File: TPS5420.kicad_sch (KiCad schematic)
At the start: 10 parts, among them U1 TPS5420D, U2 CDBC560-G

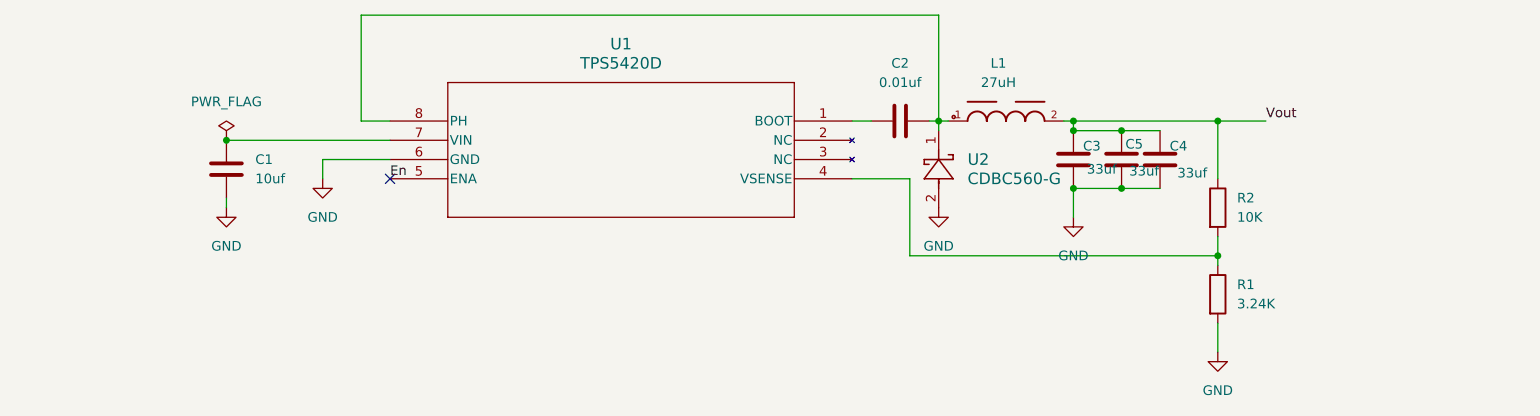
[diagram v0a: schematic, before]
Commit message: Added scre terminals
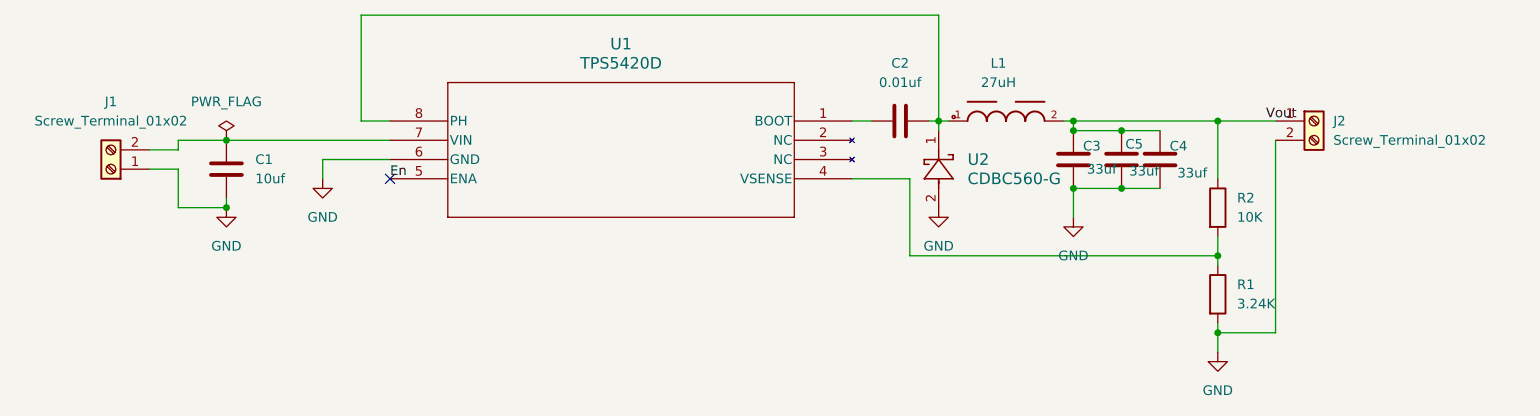
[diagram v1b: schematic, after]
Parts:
- added J1, J2: Screw_Terminal_01x02, TerminalBlock_RND:TerminalBlock_RND_205-00232_1x02_P5.08mm_Horizontal, symbol Connector:Screw_Terminal_01x02
- U2: footprint TPS5420_CADs:CDBC-G-M -> TPS5420_CADs:CDBC-G
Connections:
- net GND: now also J1.1 (Pin_1), J2.2 (Pin_2)
- net Vout: now also J2.1 (Pin_1)
- net at C1.1, U1.7 (VIN): now also J1.2 (Pin_2)
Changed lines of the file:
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@@
+	)
+	(junction
+		(at 50.8 111.76)
+		(diameter 0)
+		(color 0 0 0 0)
+	)
+	(junction
+		(at 181.61 128.27)
+		(diameter 0)
+		(color 0 0 0 0)
 	)
 	(junction
@@
 	(wire
 		(pts
+			(xy 40.64 106.68) (xy 44.45 106.68)
+		)
+		(stroke
+			(width 0)
+			(type default)
+		)
+	)
+	(wire
+		(pts
 			(xy 162.56 109.22) (xy 168.91 109.22)
 		)
@@
 	(wire
 		(pts
-			(xy 181.61 100.33) (xy 187.96 100.33)
-		)
-		(stroke
-			(width 0)
-			(type default)
-		)
-	)
-	(wire
-		(pts
 			(xy 68.58 100.33) (xy 68.58 86.36)
 		)
@@
 	(wire
 		(pts
+			(xy 189.23 128.27) (xy 181.61 128.27)
+		)
+		(stroke
+			(width 0)
+			(type default)
+		)
+	)
+	(wire
+		(pts
 			(xy 133.35 107.95) (xy 140.97 107.95)
 		)
@@
 	(wire
 		(pts
+			(xy 44.45 111.76) (xy 50.8 111.76)
+		)
+		(stroke
+			(width 0)
+			(type default)
+		)
+	)
+	(wire
+		(pts
 			(xy 140.97 107.95) (xy 140.97 118.11)
 		)
@@
 	(wire
 		(pts
+			(xy 44.45 102.87) (xy 50.8 102.87)
+		)
+		(stroke
+			(width 0)
+			(type default)
+		)
+	)
+	(wire
+		(pts
 			(xy 143.51 100.33) (xy 144.78 100.33)
 		)
@@
 	(wire
 		(pts
+			(xy 44.45 106.68) (xy 44.45 111.76)
+		)
+		(stroke
+			(width 0)
+			(type default)
+		)
+	)
+	(wire
+		(pts
+			(xy 40.64 104.14) (xy 44.45 104.14)
+		)
+		(stroke
+			(width 0)
+			(type default)
+		)
+	)
+	(wire
+		(pts
 			(xy 144.78 100.33) (xy 146.05 100.33)
 		)
@@
 	(wire
 		(pts
+			(xy 189.23 102.87) (xy 189.23 128.27)
+		)
+		(stroke
+			(width 0)
+			(type default)
+		)
+	)
+	(wire
+		(pts
+			(xy 181.61 100.33) (xy 189.23 100.33)
+		)
+		(stroke
+			(width 0)
+			(type default)
+		)
+	)
+	(wire
+		(pts
+			(xy 181.61 128.27) (xy 181.61 130.81)
+		)
+		(stroke
+			(width 0)
+			(type default)
+		)
+	)
+	(wire
+		(pts
 			(xy 50.8 110.49) (xy 50.8 111.76)
 		)
@@
 	(wire
 		(pts
+			(xy 44.45 104.14) (xy 44.45 102.87)
+		)
+		(stroke
+			(width 0)
+			(type default)
+		)
+	)
+	(wire
+		(pts
 			(xy 162.56 100.33) (xy 162.56 101.6)
 		)
@@
 	(wire
 		(pts
-			(xy 181.61 127) (xy 181.61 130.81)
+			(xy 181.61 127) (xy 181.61 128.27)
+		)
+		(stroke
+			(width 0)
+			(type default)
+		)
+	)
+	(wire
+		(pts
+			(xy 168.91 101.6) (xy 173.99 101.6)
+		)
+		(stroke
+			(width 0)
+			(type default)
+		)
+	)
+	(wire
+		(pts
+			(xy 181.61 115.57) (xy 181.61 118.11)
 		)
 		(stroke
@@
 		(pts
 			(xy 50.8 102.87) (xy 72.39 102.87)
-		)
-		(stroke
-			(width 0)
-			(type default)
-		)
-	)
-	(wire
-		(pts
-			(xy 168.91 101.6) (xy 173.99 101.6)
-		)
-		(stroke
-			(width 0)
-			(type default)
-		)
-	)
-	(wire
-		(pts
-			(xy 181.61 115.57) (xy 181.61 118.11)
 		)
 		(stroke
@@
 	)
 	(symbol
+		(lib_id "Connector:Screw_Terminal_01x02")
+		(at 35.56 106.68 180)
+		(unit 1)
+		(exclude_from_sim no)
+		(in_bom yes)
+		(on_board yes)
+		(dnp no)
+		(fields_autoplaced yes)
+		(property "Reference" "J1"
+			(at 35.56 97.79 0)
+			(effects
+				(font
+					(size 1.27 1.27)
+				)
+			)
+		)
+		(property "Value" "Screw_Terminal_01x02"
+			(at 35.56 100.33 0)
+			(effects
+				(font
+					(size 1.27 1.27)
+				)
+			)
+		)
+		(property "Footprint" "TerminalBlock_RND:TerminalBlock_RND_205-00232_1x02_P5.08mm_Horizontal"
+			(at 35.56 106.68 0)
+			(effects
+				(font
+					(size 1.27 1.27)
+				)
+				(hide yes)
+			)
+		)
+		(property "Datasheet" "~"
+			(at 35.56 106.68 0)
+			(effects
+				(font
+					(size 1.27 1.27)
+				)
+				(hide yes)
+			)
+		)
+		(property "Description" "Generic screw terminal, single row, 01x02, script generated (kicad-library-utils/schlib/autogen/connector/)"
+			(at 35.56 106.68 0)
+			(effects
+				(font
+					(size 1.27 1.27)
+				)
+				(hide yes)
+			)
+		)
+		(pin "1"
+		)
+		(pin "2"
+		)
+		(instances
+			(project ""
+				(path "/52b0f5ba-f92b-45be-b124-e7f84f7c41b2"
+					(reference "J1")
+					(unit 1)
+				)
+			)
+		)
+	)
+	(symbol
 		(lib_id "TPS5420:TPS5420D")
 		(at 133.35 100.33 0)
@@
 			)
 		)
-		(property "Footprint" "TPS5420_CADs:CDBC-G-M"
+		(property "Footprint" "TPS5420_CADs:CDBC-G"
 			(at 144.78 101.6 0)
 			(effects
@@
 					(unit 1)
 				)
+			)
+		)
+	)
+	(symbol
+		(lib_id "Connector:Screw_Terminal_01x02")
+		(at 194.31 100.33 0)
+		(unit 1)
+		(exclude_from_sim no)
+		(in_bom yes)
+		(on_board yes)
+		(dnp no)
+		(fields_autoplaced yes)
+		(property "Reference" "J2"
+			(at 196.85 100.3299 0)
+			(effects
+				(font
+					(size 1.27 1.27)
+				)
+				(justify left)
+			)
+		)
+		(property "Value" "Screw_Terminal_01x02"
+			(at 196.85 102.8699 0)
+			(effects
+				(font
+					(size 1.27 1.27)
+				)
+				(justify left)
+			)
+		)
+		(property "Footprint" "TerminalBlock_RND:TerminalBlock_RND_205-00232_1x02_P5.08mm_Horizontal"
+			(at 194.31 100.33 0)
+			(effects
+				(font
+					(size 1.27 1.27)
+				)
+				(hide yes)
+			)
+		)
+		(property "Datasheet" "~"
+			(at 194.31 100.33 0)
+			(effects
+				(font
+					(size 1.27 1.27)
+				)
+				(hide yes)
+			)
+		)
+		(property "Description" "Generic screw terminal, single row, 01x02, script generated (kicad-library-utils/schlib/autogen/connector/)"
+			(at 194.31 100.33 0)
+			(effects
+				(font
+					(size 1.27 1.27)
+				)
+				(hide yes)
+			)
+		)
+		(pin "1"
+		)
+		(pin "2"
+		)
+		(instances
+			(project "TPS5420"
+				(path "/52b0f5ba-f92b-45be-b124-e7f84f7c41b2"
+					(reference "J2")
+					(unit 1)
+				)

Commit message: v
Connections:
- net GND: now also J2.1 (Pin_1); no longer J2.2 (Pin_2)
- net Vout: now also J2.2 (Pin_2); no longer J2.1 (Pin_1)
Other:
- moved on the sheet: J2
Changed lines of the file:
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@@
+	)
+	(junction
+		(at 196.85 109.22)
+		(diameter 0)
+		(color 0 0 0 0)
 	)
 	(junction
@@
 	(wire
 		(pts
+			(xy 196.85 110.49) (xy 196.85 109.22)
+		)
+		(stroke
+			(width 0)
+			(type default)
+		)
+	)
+	(wire
+		(pts
 			(xy 44.45 111.76) (xy 50.8 111.76)
 		)
@@
 	(wire
 		(pts
+			(xy 189.23 109.22) (xy 190.5 109.22)
+		)
+		(stroke
+			(width 0)
+			(type default)
+		)
+	)
+	(wire
+		(pts
 			(xy 140.97 107.95) (xy 140.97 118.11)
 		)
@@
 	(wire
 		(pts
+			(xy 193.04 109.22) (xy 196.85 109.22)
+		)
+		(stroke
+			(width 0)
+			(type default)
+		)
+	)
+	(wire
+		(pts
 			(xy 181.61 100.33) (xy 181.61 107.95)
 		)
@@
 	(wire
 		(pts
+			(xy 189.23 128.27) (xy 189.23 109.22)
+		)
+		(stroke
+			(width 0)
+			(type default)
+		)
+	)
+	(wire
+		(pts
 			(xy 161.29 100.33) (xy 162.56 100.33)
 		)
@@
 	(wire
 		(pts
-			(xy 189.23 102.87) (xy 189.23 128.27)
-		)
-		(stroke
-			(width 0)
-			(type default)
-		)
-	)
-	(wire
-		(pts
-			(xy 181.61 100.33) (xy 189.23 100.33)
+			(xy 196.85 109.22) (xy 196.85 100.33)
 		)
 		(stroke
@@
 		(pts
 			(xy 181.61 118.11) (xy 181.61 119.38)
+		)
+		(stroke
+			(width 0)
+			(type default)
+		)
+	)
+	(wire
+		(pts
+			(xy 181.61 100.33) (xy 196.85 100.33)
 		)
 		(stroke
@@
 	)
 	(label "Vout"
-		(at 187.96 100.33 0)
+		(at 196.85 110.49 0)
 		(effects
 			(font
@@
 	(symbol
 		(lib_id "Connector:Screw_Terminal_01x02")
-		(at 194.31 100.33 0)
+		(at 190.5 104.14 90)
 		(unit 1)
 		(exclude_from_sim no)
@@
 		(fields_autoplaced yes)
 		(property "Reference" "J2"
-			(at 196.85 100.3299 0)
-			(effects
-				(font
-					(size 1.27 1.27)
-				)
-				(justify left)
+			(at 195.58 102.8699 90)
+			(effects
+				(font
+					(size 1.27 1.27)
+				)
+				(justify right)
 			)
 		)
 		(property "Value" "Screw_Terminal_01x02"
-			(at 196.85 102.8699 0)
-			(effects
-				(font
-					(size 1.27 1.27)
-				)
-				(justify left)
+			(at 195.58 105.4099 90)
+			(effects
+				(font
+					(size 1.27 1.27)
+				)
+				(justify right)
 			)
 		)
 		(property "Footprint" "TerminalBlock_RND:TerminalBlock_RND_205-00232_1x02_P5.08mm_Horizontal"
-			(at 194.31 100.33 0)
+			(at 190.5 104.14 0)
 			(effects
 				(font
@@
 		)
 		(property "Datasheet" "~"
-			(at 194.31 100.33 0)
+			(at 190.5 104.14 0)
 			(effects
 				(font
@@
 		)
 		(property "Description" "Generic screw terminal, single row, 01x02, script generated (kicad-library-utils/schlib/autogen/connector/)"
-			(at 194.31 100.33 0)
-			(effects
-				(font
+			(at 190.5 104.14 0)
+			(effects
+				(font

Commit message: SHifted out capacitors
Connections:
- net GND: now also J2.2 (Pin_2); no longer J2.1 (Pin_1)
- net Vout: now also J2.1 (Pin_1); no longer J2.2 (Pin_2)
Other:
- moved on the sheet: J2
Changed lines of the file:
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@@
+	)
+	(junction
+		(at 63.5 105.41)
+		(diameter 0)
+		(color 0 0 0 0)
 	)
 	(junction
@@
 	(symbol
 		(lib_id "Connector:Screw_Terminal_01x02")
-		(at 190.5 104.14 90)
+		(at 193.04 114.3 270)
 		(unit 1)
 		(exclude_from_sim no)
@@
 		(fields_autoplaced yes)
 		(property "Reference" "J2"
-			(at 195.58 102.8699 90)
-			(effects
-				(font
-					(size 1.27 1.27)
-				)
-				(justify right)
+			(at 195.58 113.0299 90)
+			(effects
+				(font
+					(size 1.27 1.27)
+				)
+				(justify left)
 			)
 		)
 		(property "Value" "Screw_Terminal_01x02"
-			(at 195.58 105.4099 90)
-			(effects
-				(font
-					(size 1.27 1.27)
-				)
-				(justify right)
+			(at 195.58 115.5699 90)
+			(effects
+				(font
+					(size 1.27 1.27)
+				)
+				(justify left)
 			)
 		)
 		(property "Footprint" "TerminalBlock_RND:TerminalBlock_RND_205-00232_1x02_P5.08mm_Horizontal"
-			(at 190.5 104.14 0)
+			(at 193.04 114.3 0)
 			(effects
 				(font
@@
 		)
 		(property "Datasheet" "~"
-			(at 190.5 104.14 0)
+			(at 193.04 114.3 0)
 			(effects
 				(font
@@
 		)
 		(property "Description" "Generic screw terminal, single row, 01x02, script generated (kicad-library-utils/schlib/autogen/connector/)"
-			(at 190.5 104.14 0)
+			(at 193.04 114.3 0)
 			(effects
 				(font
@@
 					(unit 1)
 				)
+			)
+		)
+	)
+	(symbol
+		(lib_id "power:PWR_FLAG")
+		(at 63.5 105.41 0)
+		(unit 1)
+		(exclude_from_sim no)
+		(in_bom yes)
+		(on_board yes)
+		(dnp no)
+		(fields_autoplaced yes)
+		(property "Reference" "#FLG02"
+			(at 63.5 103.505 0)
+			(effects
+				(font
+					(size 1.27 1.27)
+				)
+				(hide yes)
+			)
+		)
+		(property "Value" "PWR_FLAG"
+			(at 63.5 100.33 0)
+			(effects
+				(font
+					(size 1.27 1.27)
+				)
+			)
+		)
+		(property "Footprint" ""
+			(at 63.5 105.41 0)
+			(effects
+				(font
+					(size 1.27 1.27)
+				)
+				(hide yes)
+			)
+		)
+		(property "Datasheet" "~"
+			(at 63.5 105.41 0)
+			(effects
+				(font
+					(size 1.27 1.27)
+				)
+				(hide yes)
+			)
+		)
+		(property "Description" "Special symbol for telling ERC where power comes from"
+			(at 63.5 105.41 0)
+			(effects
+				(font
+					(size 1.27 1.27)
+				)
+				(hide yes)
+			)
+		)
+		(pin "1"
+		)
+		(instances
+			(project ""
+				(path "/52b0f5ba-f92b-45be-b124-e7f84f7c41b2"
+					(reference "#FLG02")
+					(unit 1)
+				)
